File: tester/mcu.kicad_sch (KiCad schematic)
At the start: 38 parts, among them J201 PWR, J202 SWD, Q201 SI2301CDS-T1-GE3, SW201 Reset, U201 AMS1117-3.3, U202 STM32F103C8Tx, U203 M24C64-RMN, U204 M24C64-RMN, Y201 8MHz, Y202 32k

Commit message: Add automation for tester
Signed-off-by: Benedikt Spranger <b.spranger@linutronix.de>
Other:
- company: (none) -> Benedikt Spranger
- title: (none) -> rack-ser-adapter-tester
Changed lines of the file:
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@@
 	(generator_version "10.0")
 	(paper "A4")
+	(title_block
+		(title "rack-ser-adapter-tester")
+		(date "2026-09-15")
+		(rev "v0.1")
+		(company "Benedikt Spranger")
+		(comment 1 "SPDX-License-Identifier: CERN-OHL-S-2.0")
+		(comment 2 "https://ohwr.org/cern_ohl_s_v2.txt")
+		(comment 3 "To view a copy of this license, visit")
+		(comment 4 "This work is licensed under the CERN-OHL-S v2")
+	)
 	(junction
 		(at 116.84 68.58)

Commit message: Use correct part for D201
Signed-off-by: Benedikt Spranger <b.spranger@linutronix.de>
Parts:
- D201: LCSC# C2128 -> C81598; Long Description 1.25V@150mA 100V 150mA 1uA@75V 200mW 2A 4ns Independent SOD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 -> 150mA 1A 1V@50mA 1uA@75V 400mW 4ns 75V Independent SOD-123 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; MF Jiangsu Changjing Electronics Technology Co., Ltd. -> ST(Semtech); MP 1N4148WS -> 1N4148W; Manufacture Jiangsu Changjing Electronics Technology Co., Ltd. -> ST(Semtech); mpn 1N4148WS -> 1N4148W
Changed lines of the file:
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@@
 			)
 		)
-		(property "Long Description" " 1.25V@150mA 100V 150mA 1uA@75V 200mW 2A 4ns Independent SOD-323 Switching Diodes ROHS"
+		(property "Long Description" "150mA 1A 1V@50mA 1uA@75V 400mW 4ns 75V Independent SOD-123 Switching Diodes ROHS"
 			(at 114.3 31.75 90)
 			(hide yes)
@@
 			)
 		)
-		(property "MF" "Jiangsu Changjing Electronics Technology Co., Ltd."
+		(property "MF" "ST(Semtech)"
 			(at 114.3 31.75 90)
 			(hide yes)
@@
 			)
 		)
-		(property "MP" "1N4148WS"
+		(property "MP" "1N4148W"
 			(at 114.3 31.75 90)
 			(hide yes)
@@
 			)
 		)
-		(property "LCSC#" "C2128"
+		(property "LCSC#" "C81598"
 			(at 114.3 31.75 90)
 			(hide yes)
@@
 			)
 		)
-		(property "Manufacture" "Jiangsu Changjing Electronics Technology Co., Ltd."
+		(property "Manufacture" "ST(Semtech)"
 			(at 114.3 31.75 90)
 			(hide yes)
@@
 			)
 		)
-		(property "mpn" "1N4148WS"
+		(property "mpn" "1N4148W"
 			(at 114.3 31.75 90)
 			(hide yes)

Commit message: Fix SWD
Signed-off-by: Benedikt Spranger <b.spranger@linutronix.de>
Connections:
- net SYS_SWDIO: now also U202.34 (PA13); no longer U202.38 (PA15)
- net ~{RST1}: now also U202.25 (PB12); no longer U202.34 (PA13)
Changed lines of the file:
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@@
 	)
 	(no_connect
-		(at 139.7 111.76)
+		(at 175.26 91.44)
 	)
 	(wire
@@
 	(wire
 		(pts
+			(xy 137.16 111.76) (xy 139.7 111.76)
+		)
+		(stroke
+			(width 0)
+			(type default)
+		)
+	)
+	(wire
+		(pts
 			(xy 63.5 96.52) (xy 63.5 99.06)
 		)
@@
 		(pts
 			(xy 58.42 38.1) (xy 58.42 40.64)
-		)
-		(stroke
-			(width 0)
-			(type default)
-		)
-	)
-	(wire
-		(pts
-			(xy 175.26 91.44) (xy 177.8 91.44)
 		)
 		(stroke
@@
 	)
 	(label "SYS_SWDIO"
-		(at 177.8 91.44 0)
+		(at 177.8 86.36 0)
 		(effects
 			(font
@@
 	(hierarchical_label "~{RST1}"
 		(shape output)
-		(at 177.8 86.36 0)
-		(effects
-			(font
-				(size 1.27 1.27)
-			)
-			(justify left)
-		)
-	)
+		(at 137.16 111.76 180)
+		(effects
+			(font
+				(size 1.27 1.27)
+			)
+			(justify right)
+		)
+	)

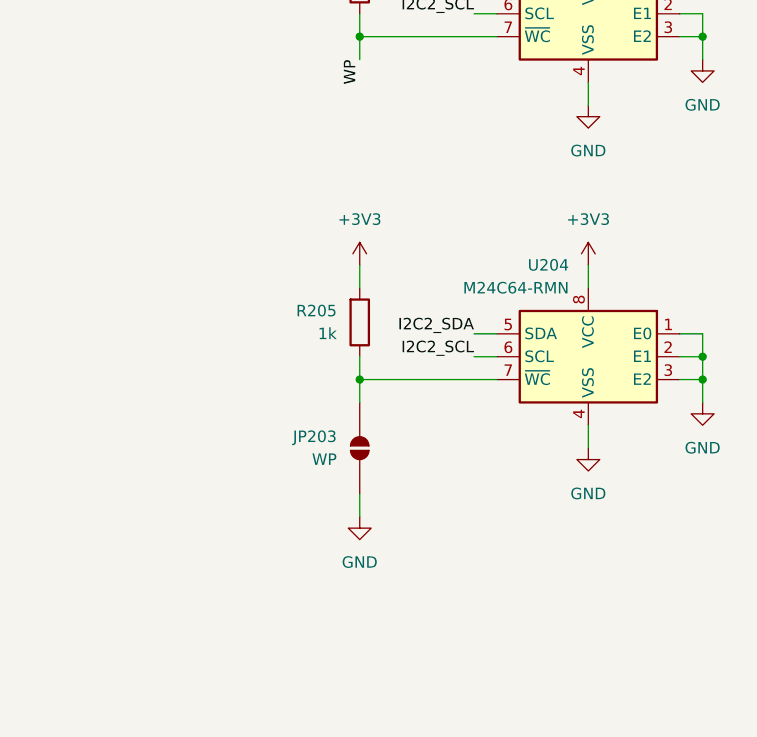
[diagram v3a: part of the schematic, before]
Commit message: Add missing I2C pullups
Signed-off-by: Benedikt Spranger <b.spranger@linutronix.de>
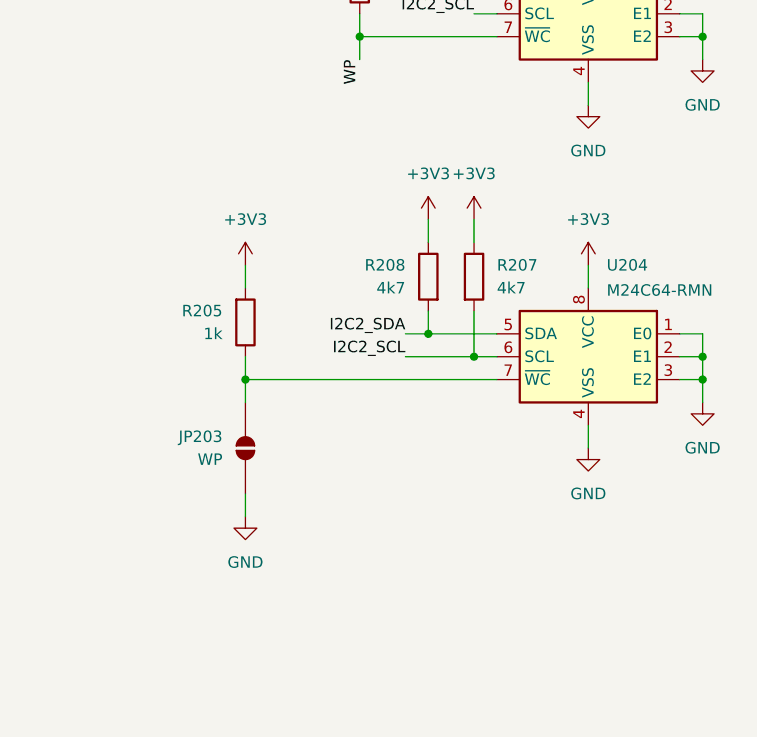
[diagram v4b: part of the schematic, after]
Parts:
- added R207, R208: 4k7, Resistor_SMD:R_0402_1005Metric, symbol Device:R
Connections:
- net +3V3: now also R207.1, R208.1
- net I2C2_SCL: now also R207.2
- net I2C2_SDA: now also R208.2
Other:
- moved on the sheet: JP203, R205

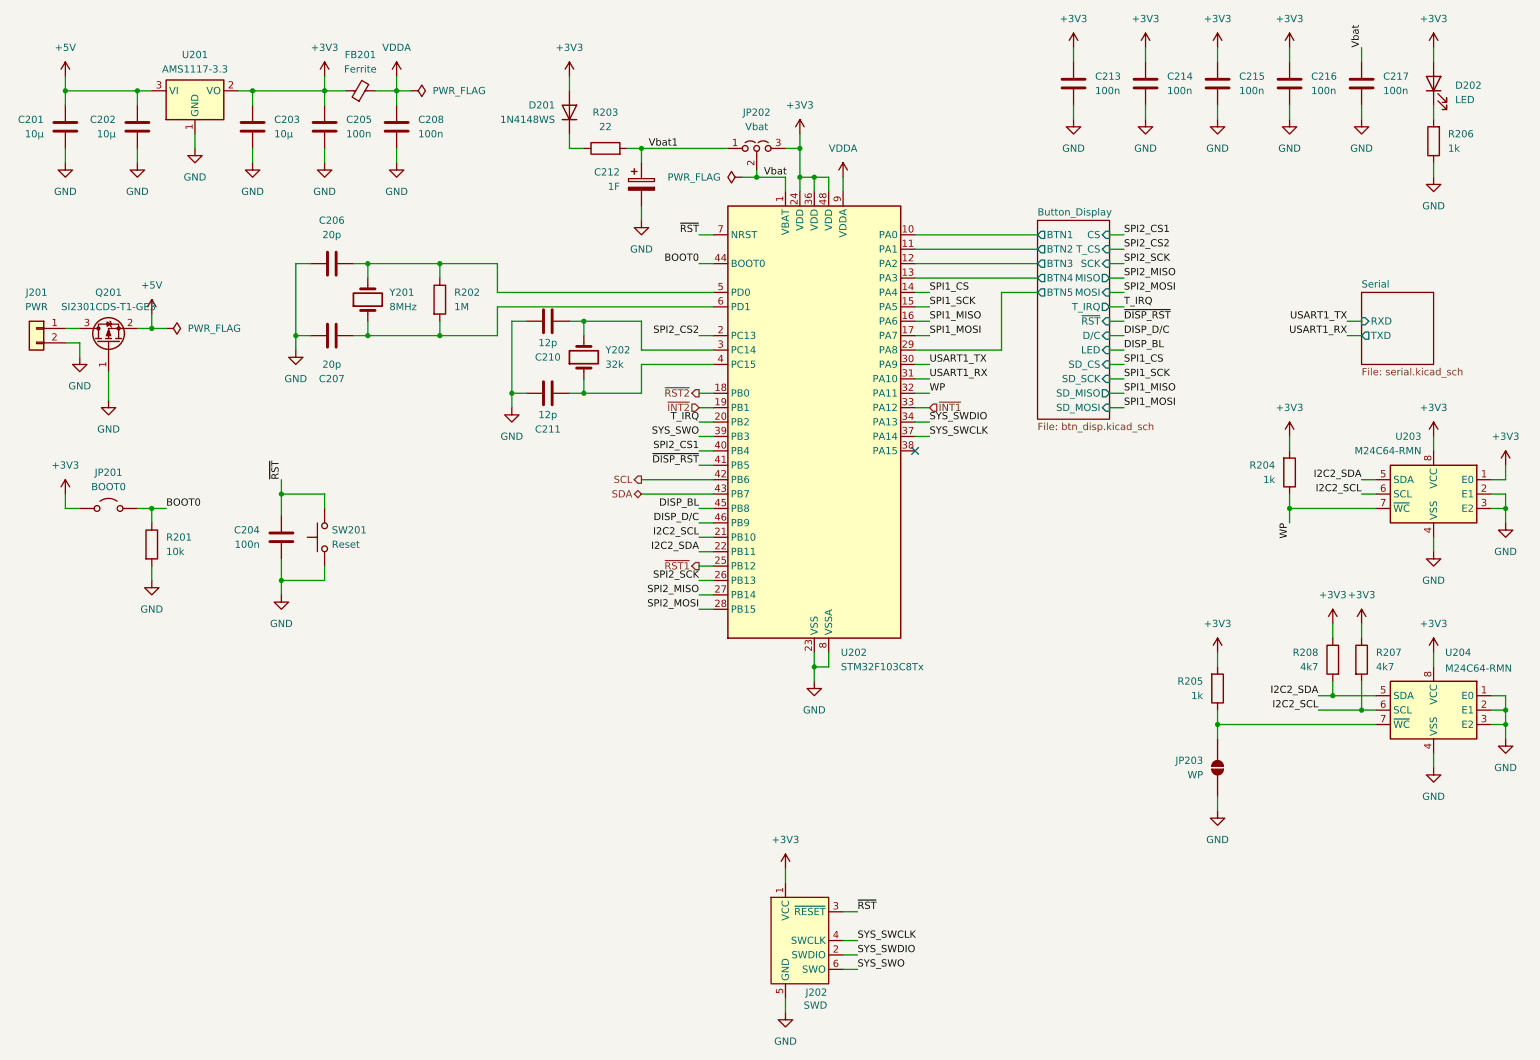
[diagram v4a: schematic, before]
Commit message: Add LDO recommended tantalum capacitor
Signed-off-by: Benedikt Spranger <b.spranger@linutronix.de>
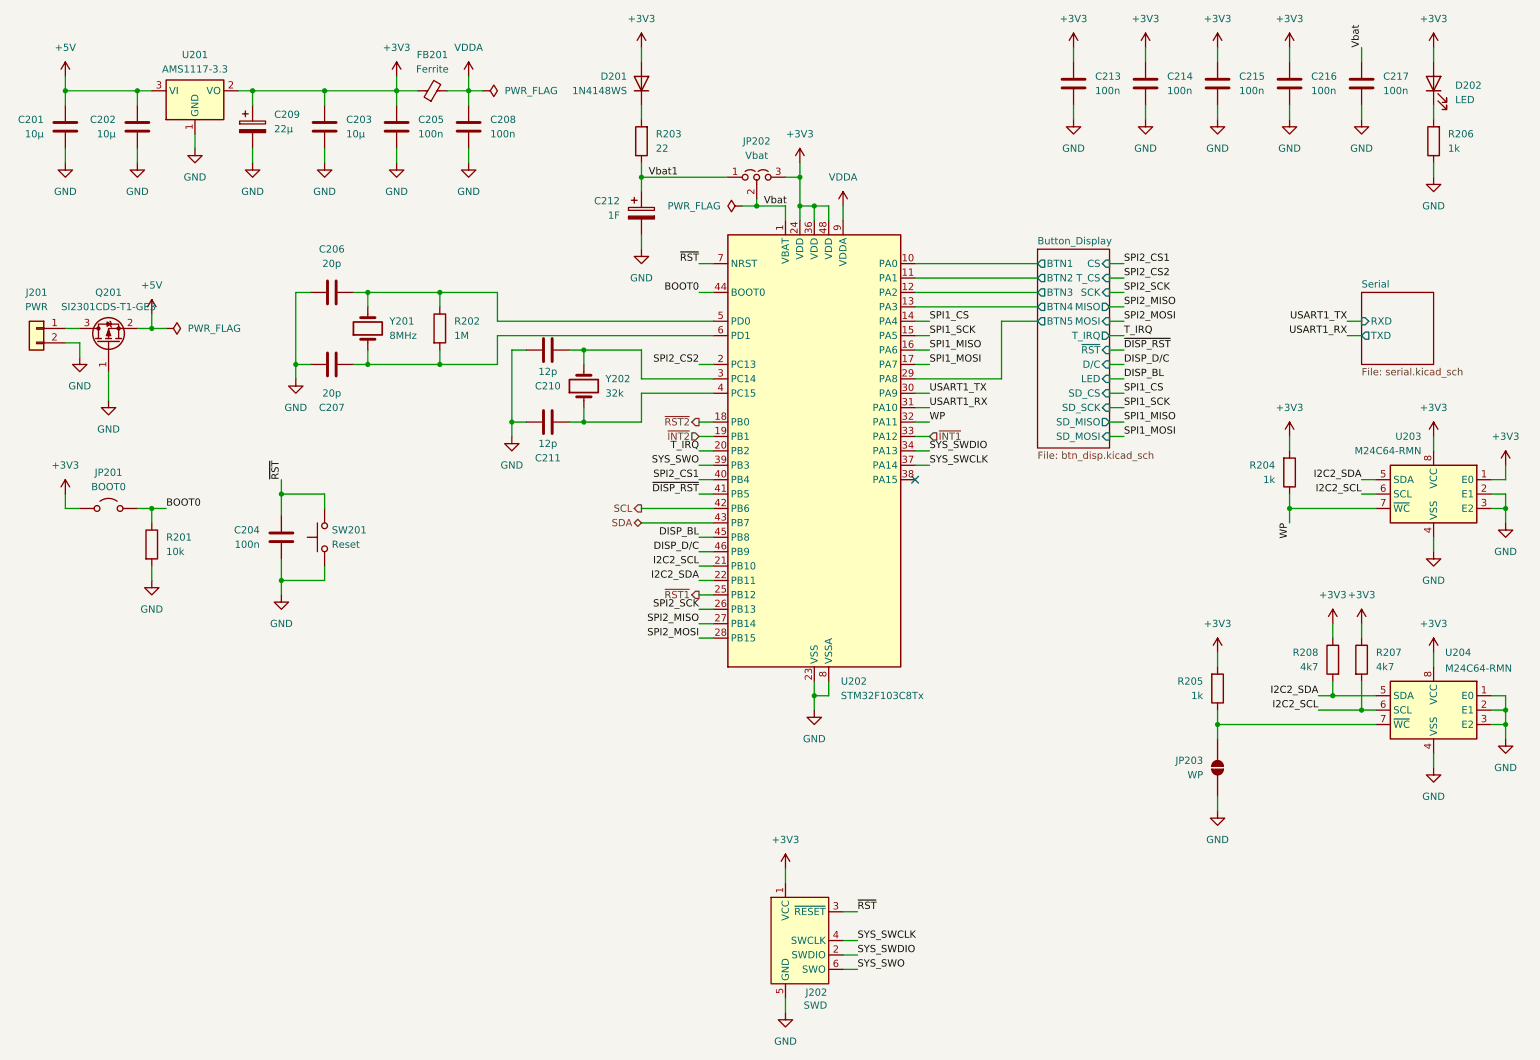
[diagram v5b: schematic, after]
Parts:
- added C209: 22µ, Capacitor_Tantalum_SMD:CP_EIA-3216-18_Kemet-A, symbol Device:C_Polarized
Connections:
- net +3V3: now also C209.1
- net GND: now also C209.2
- net Vbat1: now also R203.1; no longer R203.2
- net at D201.1 (K): now also R203.2; no longer R203.1
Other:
- moved on the sheet: C203, C205, C206, C207, C208, C210, C211, C212, D201, FB201, JP202, R202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
